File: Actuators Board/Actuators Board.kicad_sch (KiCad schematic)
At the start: 70 parts, among them IC1 BD62120AEFJ-E2, J1 Conn_01x05_Male, J10 Conn_01x02_Male, J2 Solenoid(Sol), J4 Conn_01x03_Male, J5 Conn_01x06_Male, J9 Conn_01x02_Male, Q1 MMDT2222A, Q2 SI2366DS, U1 ESP32-PICO-D4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

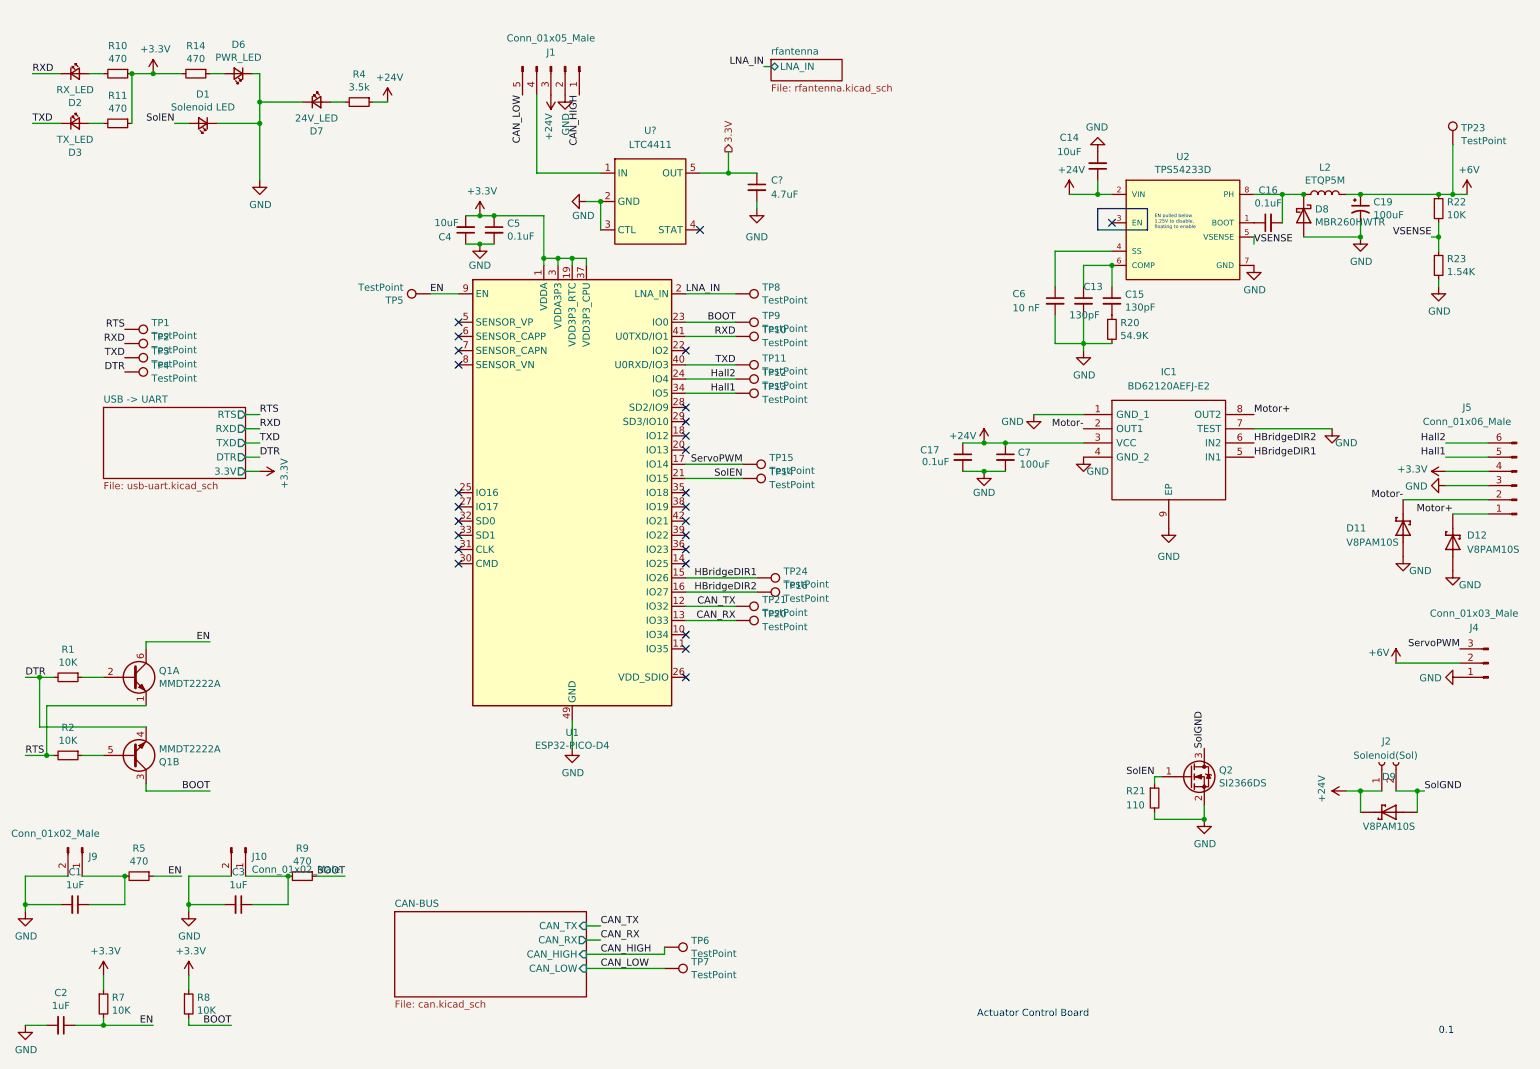
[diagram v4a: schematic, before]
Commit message: Manual merge of ideal diodes and footprint changes
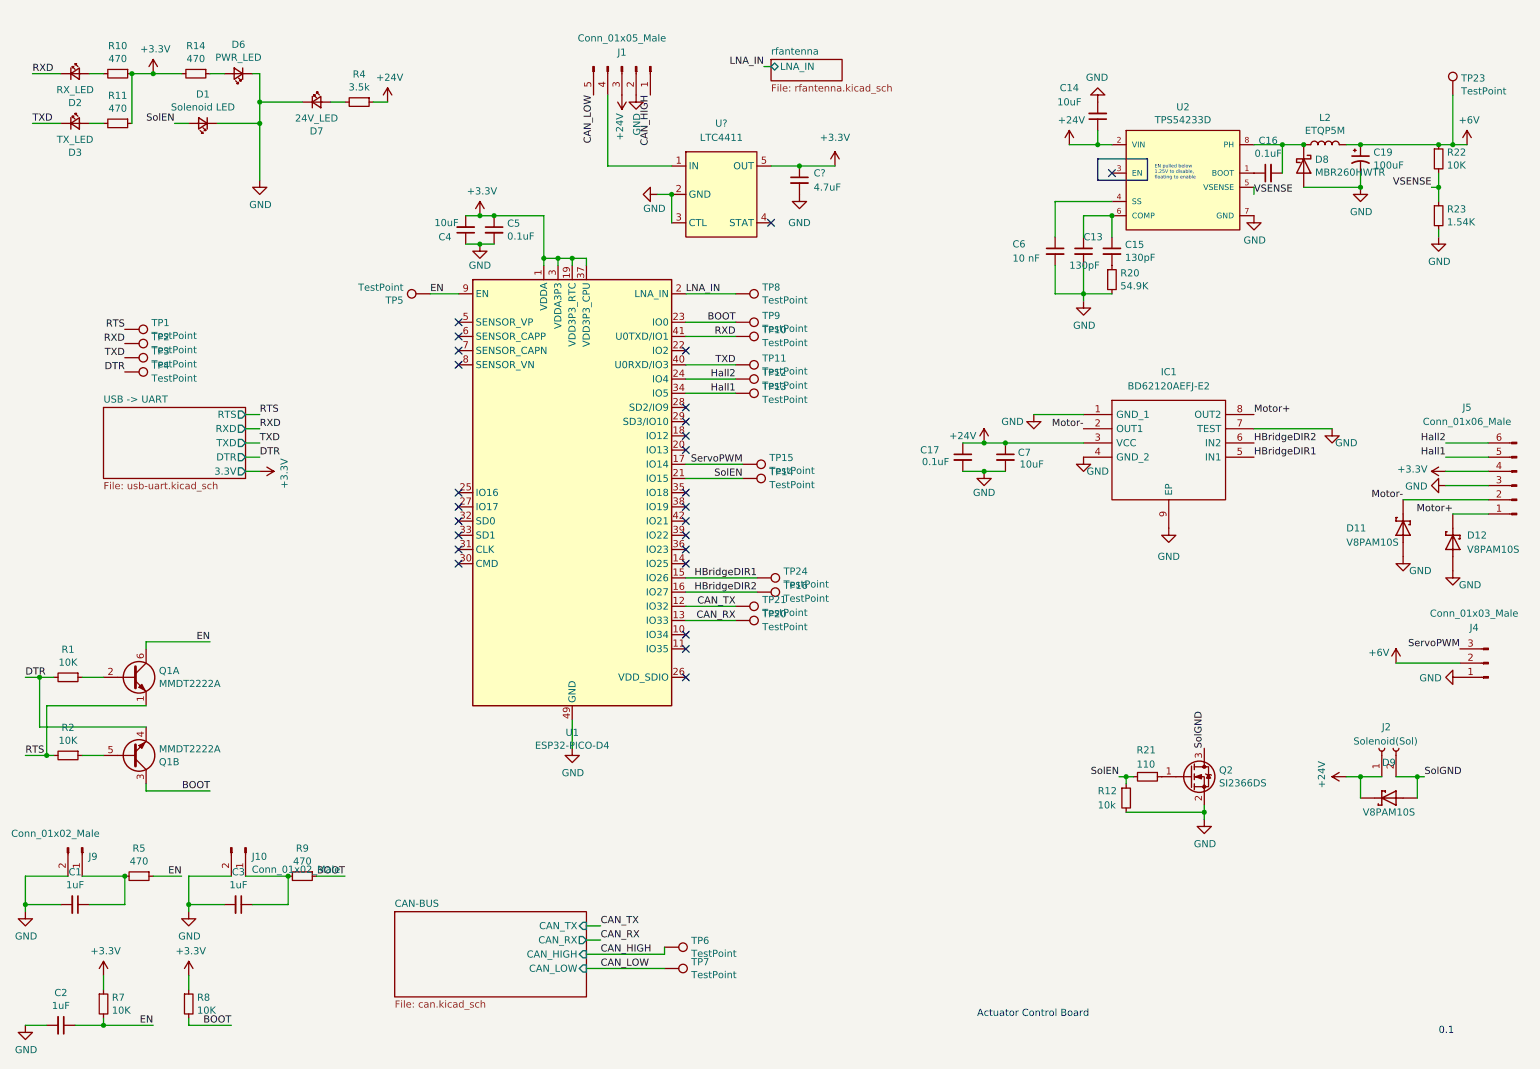
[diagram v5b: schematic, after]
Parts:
- removed C?: 4.7uF, symbol Device:C_Small
- removed U?: LTC4411, symbol iclr:LTC4411
- added C?: 4.7uF, symbol Device:C_Small
- added R12: 10k, Resistor_SMD:R_0603_1608Metric, symbol Device:R_Small
- added U?: LTC4411, symbol iclr:LTC4411
- C14: footprint Capacitor_SMD:C_0603_1608Metric -> Capacitor_SMD:C_1210_3225Metric
- C7: value 100uF -> 10uF; footprint Capacitor_SMD:C_0603_1608Metric -> Capacitor_SMD:C_1210_3225Metric
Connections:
- net +3V3: now also C?.1, U?.5 (OUT)
- net GND: now also C?.2, R12.2, U?.2 (GND), U?.3 (CTL); no longer R21.2
- net SolEN: now also R21.2, R12.1; no longer Q2.1 (G), R21.1
- net at J1.4 (Pin_4): now also U?.1 (IN)
- new net: Q2.1 (G), R21.1
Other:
- moved on the sheet: C13, C14, C15, C16, C19, C6, D8, D9, J1, J2, L2, R20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

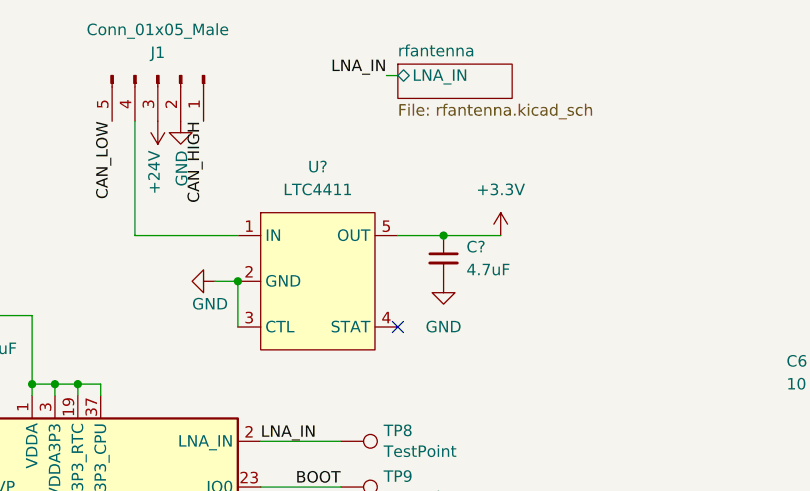
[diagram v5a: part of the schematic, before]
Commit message: Annotated schematic and imported changes into PCB
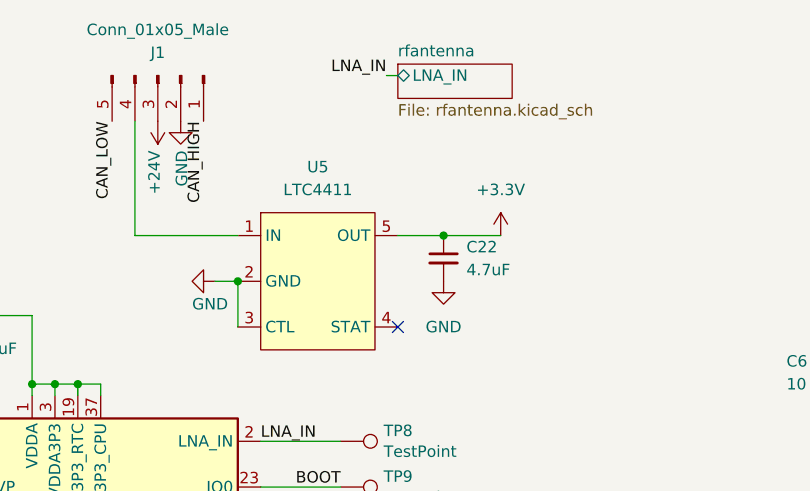
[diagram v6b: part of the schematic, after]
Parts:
- C22: renamed from C?; footprint (none) -> Capacitor_SMD:C_0603_1608Metric
- U5: renamed from U?; footprint (none) -> Package_TO_SOT_SMD:SOT-23-5
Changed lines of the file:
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@@
   (symbol (lib_id "iclr:LTC4411") (at 140.97 33.02 0) (unit 1)
     (in_bom yes) (on_board yes) (fields_autoplaced)
-    (property "Reference" "U?" (id 0) (at 140.97 30.48 0))
+    (property "Reference" "U5" (id 0) (at 140.97 30.48 0))
     (property "Value" "LTC4411" (id 1) (at 140.97 33.02 0))
-    (property "Footprint" "" (id 2) (at 140.97 33.02 0)
+    (property "Footprint" "Package_TO_SOT_SMD:SOT-23-5" (id 2) (at 140.97 33.02 0)
       (effects (font (size 1.27 1.27)) hide)
     )
@@
   (symbol (lib_id "power:GND") (at 154.94 43.18 0) (unit 1)
     (in_bom yes) (on_board yes) (fields_autoplaced)
-    (property "Reference" "#PWR?" (id 0) (at 154.94 49.53 0)
+    (property "Reference" "#PWR0140" (id 0) (at 154.94 49.53 0)
       (effects (font (size 1.27 1.27)) hide)
     )
@@
   (symbol (lib_id "power:GND") (at 129.54 43.18 270) (unit 1)
     (in_bom yes) (on_board yes)
-    (property "Reference" "#PWR?" (id 0) (at 123.19 43.18 0)
+    (property "Reference" "#PWR0148" (id 0) (at 123.19 43.18 0)
       (effects (font (size 1.27 1.27)) hide)
     )
@@
   (symbol (lib_id "Device:C_Small") (at 154.94 40.64 0) (unit 1)
     (in_bom yes) (on_board yes) (fields_autoplaced)
-    (property "Reference" "C?" (id 0) (at 157.48 39.3762 0)
+    (property "Reference" "C22" (id 0) (at 157.48 39.3762 0)
       (effects (font (size 1.27 1.27)) (justify left))
     )
@@
       (effects (font (size 1.27 1.27)) (justify left))
     )
-    (property "Footprint" "" (id 2) (at 154.94 40.64 0)
+    (property "Footprint" "Capacitor_SMD:C_0603_1608Metric" (id 2) (at 154.94 40.64 0)
       (effects (font (size 1.27 1.27)) hide)
     )
@@
   (symbol (lib_id "power:+3.3V") (at 161.29 38.1 0) (unit 1)
     (in_bom yes) (on_board yes) (fields_autoplaced)
-    (property "Reference" "#PWR?" (id 0) (at 161.29 41.91 0)
+    (property "Reference" "#PWR0147" (id 0) (at 161.29 41.91 0)
       (effects (font (size 1.27 1.27)) hide)
     )
@@
       (reference "#PWR0139") (unit 1) (value "+24V") (footprint "")
     )
+    (path "/4a32519b-38c3-4ef3-b91b-ab30c9909ae2"
+      (reference "#PWR0140") (unit 1) (value "GND") (footprint "")
+    )
     (path "/00000000-0000-0000-0000-000061be762f"
       (reference "#PWR0141") (unit 1) (value "+24V") (footprint "")
@@
       (reference "#PWR0146") (unit 1) (value "GND") (footprint "")
     )
-    (path "/4a32519b-38c3-4ef3-b91b-ab30c9909ae2"
-      (reference "#PWR?") (unit 1) (value "GND") (footprint "")
+    (path "/db7556dc-365c-4ba5-a3e8-a7992af37864"
+      (reference "#PWR0147") (unit 1) (value "+3.3V") (footprint "")
+    )
+    (path "/6a872826-c335-4683-aa10-f7bbc9966469"
+      (reference "#PWR0148") (unit 1) (value "GND") (footprint "")
+    )
+    (path "/00000000-0000-0000-0000-000061925999/bf245106-2887-49a9-af16-cd92fb99f638"
+      (reference "#PWR0149") (unit 1) (value "GND") (footprint "")
     )
     (path "/00000000-0000-0000-0000-000061925999/5d60cb60-109f-4f47-a369-e940a4c7606c"
-      (reference "#PWR?") (unit 1) (value "GND") (footprint "")
-    )
-    (path "/6a872826-c335-4683-aa10-f7bbc9966469"
-      (reference "#PWR?") (unit 1) (value "GND") (footprint "")
-    )
-    (path "/00000000-0000-0000-0000-000061925999/bf245106-2887-49a9-af16-cd92fb99f638"
-      (reference "#PWR?") (unit 1) (value "GND") (footprint "")
-    )
-    (path "/db7556dc-365c-4ba5-a3e8-a7992af37864"
-      (reference "#PWR?") (unit 1) (value "+3.3V") (footprint "")
+      (reference "#PWR0150") (unit 1) (value "GND") (footprint "")
     )
     (path "/00000000-0000-0000-0000-000061a24258/00000000-0000-0000-0000-000061a4fe29"
@@
     )
     (path "/7203a4cd-9333-480a-97ce-bf57a111c8cf"
-      (reference "C?") (unit 1) (value "4.7uF") (footprint "")
+      (reference "C22") (unit 1) (value "4.7uF") (footprint "Capacitor_SMD:C_0603_1608Metric")
     )
     (path "/00000000-0000-0000-0000-000061925999/f6d92f4e-2e3d-4f6b-8a27-5d40a9c9c758"
-      (reference "C?") (unit 1) (value "4.7uF") (footprint "")
+      (reference "C23") (unit 1) (value "4.7uF") (footprint "Capacitor_SMD:C_0603_1608Metric")
     )
     (path "/00000000-0000-0000-0000-000061db1e33"
@@
       (reference "U4") (unit 1) (value "SN65HVD230") (footprint "Package_SO:SOIC-8_3.9x4.9mm_P1.27mm")
     )
+    (path "/427435d2-68b6-463c-a7b0-b9e895f2d8c2"
+      (reference "U5") (unit 1) (value "LTC4411") (footprint "Package_TO_SOT_SMD:SOT-23-5")
+    )
     (path "/00000000-0000-0000-0000-000061925999/664ae9f5-2b0c-4b11-a427-dc1b8ed50034"
       (reference "U6") (unit 1) (value "AZ1084-3.3") (footprint "Package_TO_SOT_SMD:TO-252-3_TabPin2")
     )
     (path "/00000000-0000-0000-0000-000061925999/261fd709-b119-45e9-aff5-04154ebd9314"
-      (reference "U?") (unit 1) (value "LTC4411") (footprint "")
-    )
-    (path "/427435d2-68b6-463c-a7b0-b9e895f2d8c2"
-      (reference "U?") (unit 1) (value "LTC4411") (footprint "")
-    )
-  )
+      (reference "U7") (unit 1) (value "LTC4411") (footprint "Package_TO_SOT_SMD:SOT-23-5")
+    )
+  )

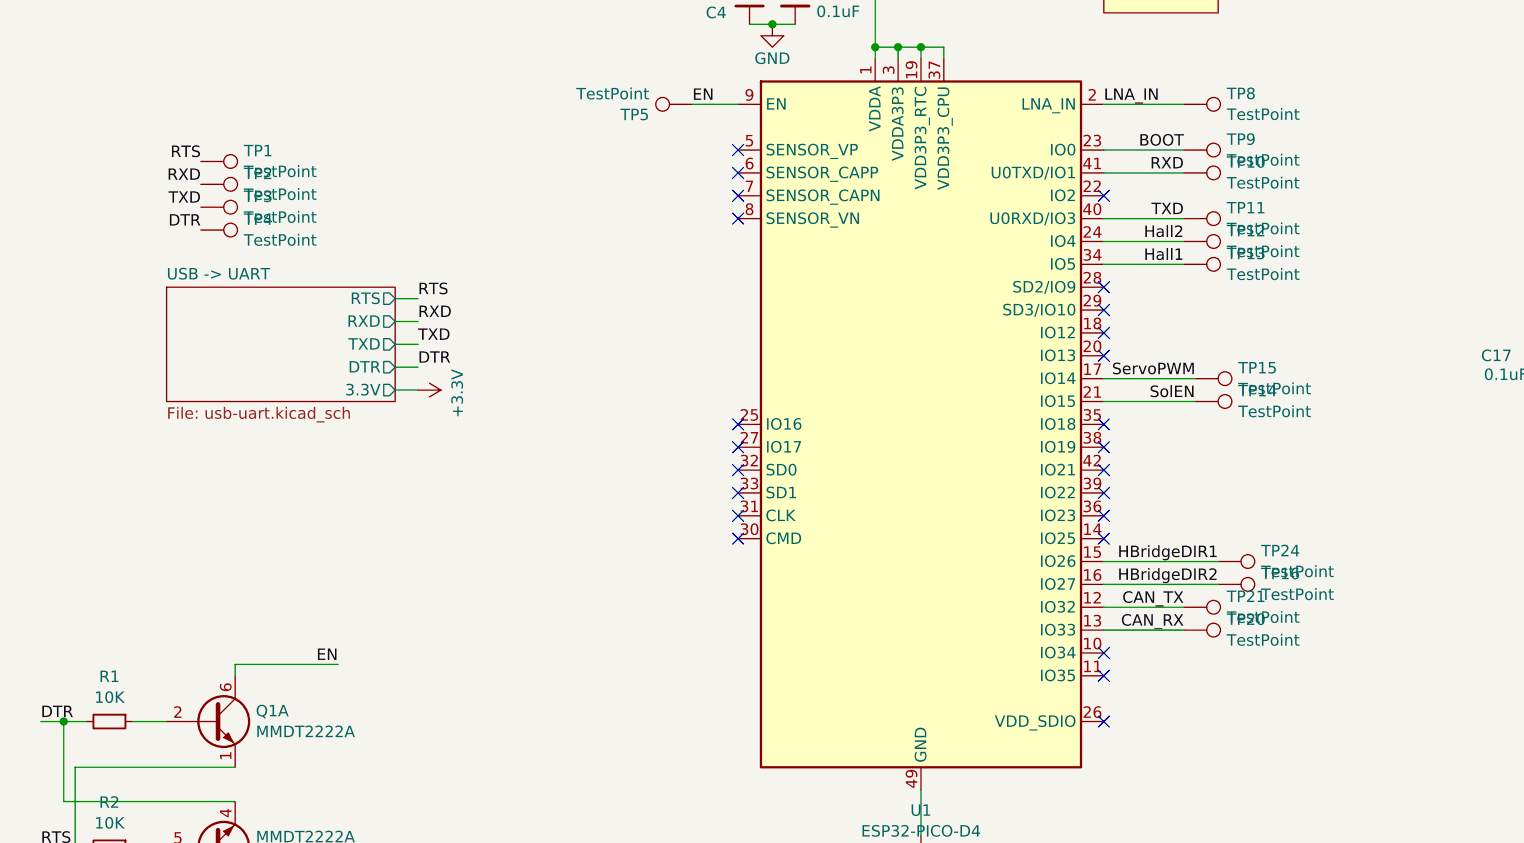
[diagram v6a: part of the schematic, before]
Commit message: H bridge & CAN Transceiver final placement
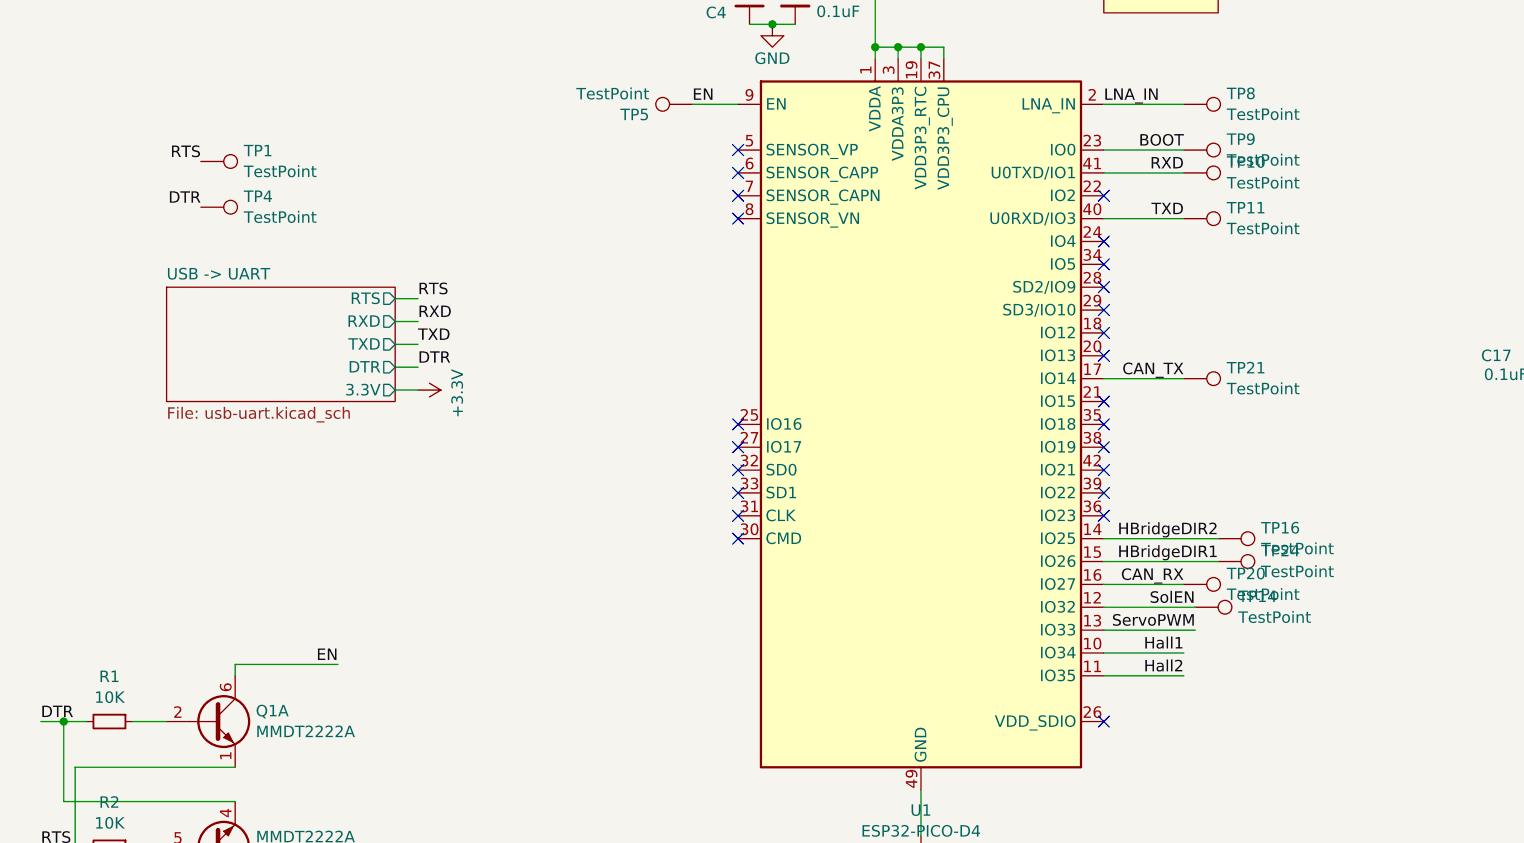
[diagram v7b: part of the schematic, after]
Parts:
- removed TP12, TP13, TP15, TP2, TP3: TestPoint, TestPoint:TestPoint_THTPad_1.0x1.0mm_Drill0.5mm, symbol Connector:TestPoint
- J5: footprint Connector_PinSocket_2.54mm:PinSocket_1x06_P2.54mm_Vertical -> Connector_PinHeader_2.54mm:PinHeader_1x06_P2.54mm_Vertical
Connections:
- net CAN_RX: now also U1.16 (IO27); no longer U1.13 (IO33)
- net CAN_TX: now also U1.17 (IO14); no longer U1.12 (IO32)
- net HBridgeDIR2: now also U1.14 (IO25); no longer U1.16 (IO27)
- net Hall1: now also U1.10 (IO34); no longer U1.34 (IO5)
- net Hall2: now also U1.11 (IO35); no longer U1.24 (IO4)
- net ServoPWM: now also U1.13 (IO33); no longer U1.17 (IO14)
- net SolEN: now also U1.12 (IO32); no longer U1.21 (IO15)
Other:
- moved on the sheet: TP14, TP16, TP20, TP21, TP4
